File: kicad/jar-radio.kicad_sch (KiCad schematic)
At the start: 65 parts, among them J1 USB-C 5V, J2 18650 holder, J3 ANT wire, J4 SPK wires, Q1 AO3401A, U1 Si4825-A10, U2 NS8002, U3 TP4056, U4 XC6206P332MR, U5 XC61CN2702MR, U6 XB8089D, Y1 32.768kHz

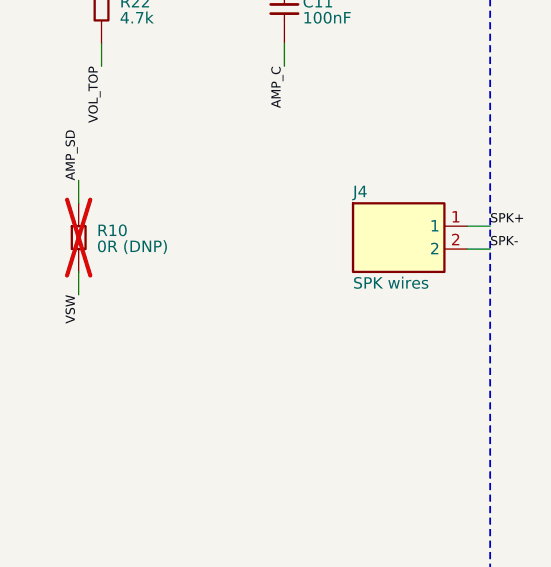
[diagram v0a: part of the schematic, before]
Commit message: Speaker top-mount: HDK-4008BB-2 soldered by its back tabs to plated pads, board cutout for cup/vents/potting; CGW logo + name on the front; outline-aware via placement; routed clean
Co-Authored-By: Claude Opus 5.5 <noreply@anthropic.com>
Claude-Session: https://claude.ai/code/session_01UChZ4MGw6SzykNSB399iC4
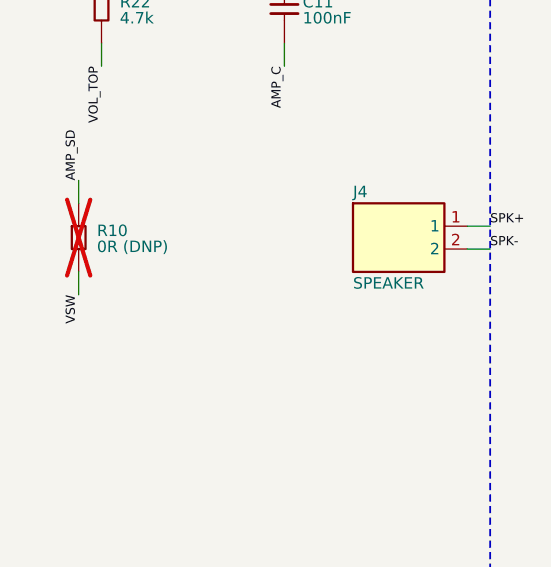
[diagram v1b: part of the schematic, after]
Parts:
- J4: value SPK wires -> SPEAKER; footprint jar-radio:Speaker_Wire_Pads_P5 -> jar-radio:Speaker_HDK-4008BB-2_TopMount; MPN HDK-4008BB-2 (hand-wired) -> HDK-4008BB-2 (C22371323, hand-soldered by its tabs)

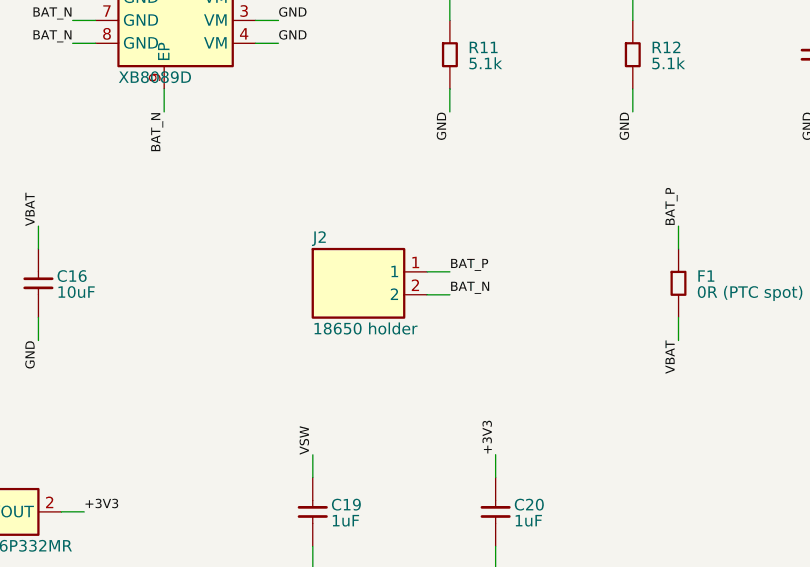
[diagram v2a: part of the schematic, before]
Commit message: Route the 102050/PH2.0 battery layout (0 unconnected); exports, renders, BOM check and plan regenerated
Co-Authored-By: Claude Opus 5.5 <noreply@anthropic.com>
Claude-Session: https://claude.ai/code/session_01UChZ4MGw6SzykNSB399iC4
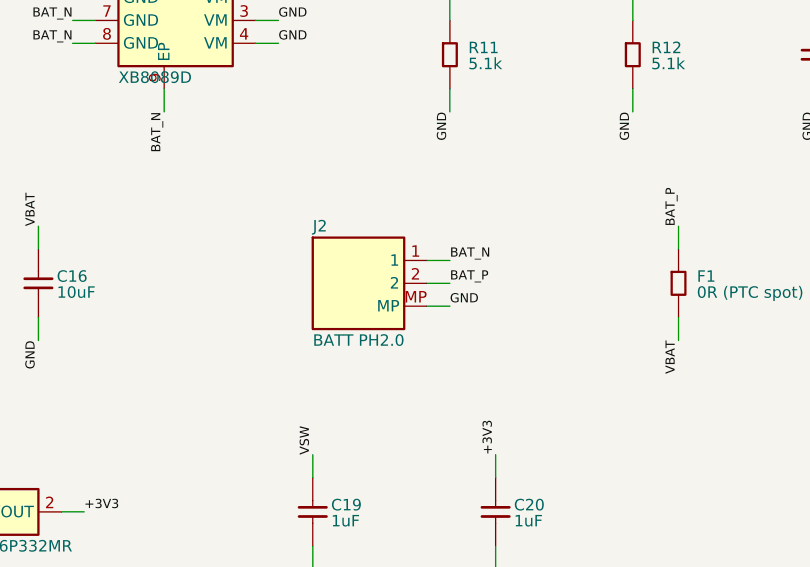
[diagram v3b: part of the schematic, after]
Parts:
- removed J2: 18650 holder, jar-radio:Battery_Holder_Tab_Slot_Plus_Wire, symbol jar-radio:Conn_2
- added J2: BATT PH2.0, jar-radio:Battery_PH2.0_RightAngle_SMD_PlugCutout, symbol jar-radio:Conn_2_MP
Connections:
- net BAT_N: now also J2.1
- net BAT_P: now also J2.2
- net GND: now also J2.MP

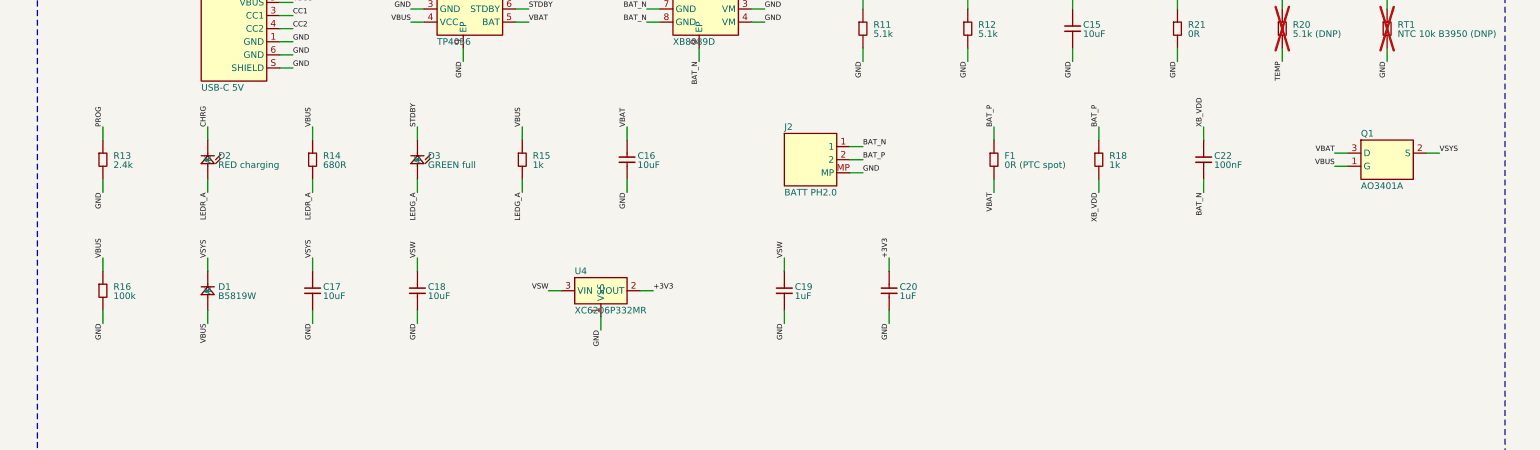
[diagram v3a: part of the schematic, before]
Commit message: Route with polarity jumpers, moved antenna hole and speaker labels (0 unconnected); exports, renders, BOM check and plan regenerated
Co-Authored-By: Claude Opus 5.5 <noreply@anthropic.com>
Claude-Session: https://claude.ai/code/session_01UChZ4MGw6SzykNSB399iC4
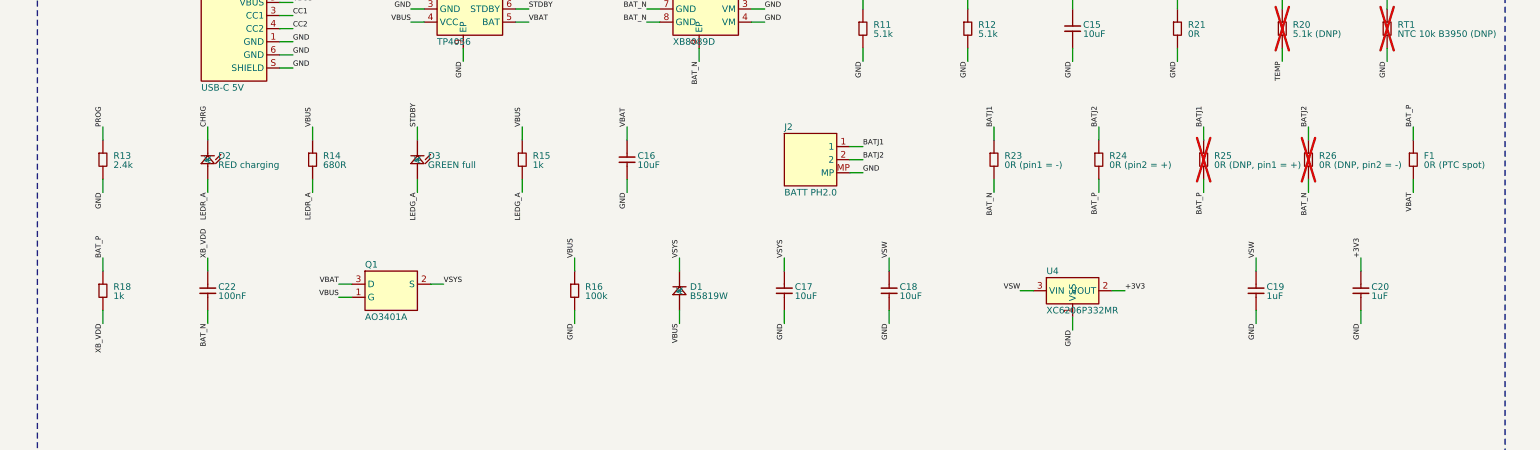
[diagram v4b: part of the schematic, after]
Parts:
- added R23: 0R (pin1 = -), Resistor_SMD:R_1206_3216Metric, symbol jar-radio:R
- added R24: 0R (pin2 = +), Resistor_SMD:R_1206_3216Metric, symbol jar-radio:R
- added R25: 0R (DNP, pin1 = +), Resistor_SMD:R_1206_3216Metric, symbol jar-radio:R
- added R26: 0R (DNP, pin2 = -), Resistor_SMD:R_1206_3216Metric, symbol jar-radio:R
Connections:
- net BAT_N: now also R23.2, R26.2; no longer J2.1
- net BAT_P: now also R24.2, R25.2; no longer J2.2
- new net BATJ1: J2.1, R23.1, R25.1
- new net BATJ2: J2.2, R24.1, R26.1
